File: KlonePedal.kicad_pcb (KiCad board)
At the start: 2 copper layers, 57.5 x 92.1 mm, 68 parts, among them J1 Jack-DC, J2 NMJ4HCD2, J4 NMJ4HCD2, SW1 SW_DPDT_x2, U1 TL072, U2 TL072, U3 MAX1044CPA+

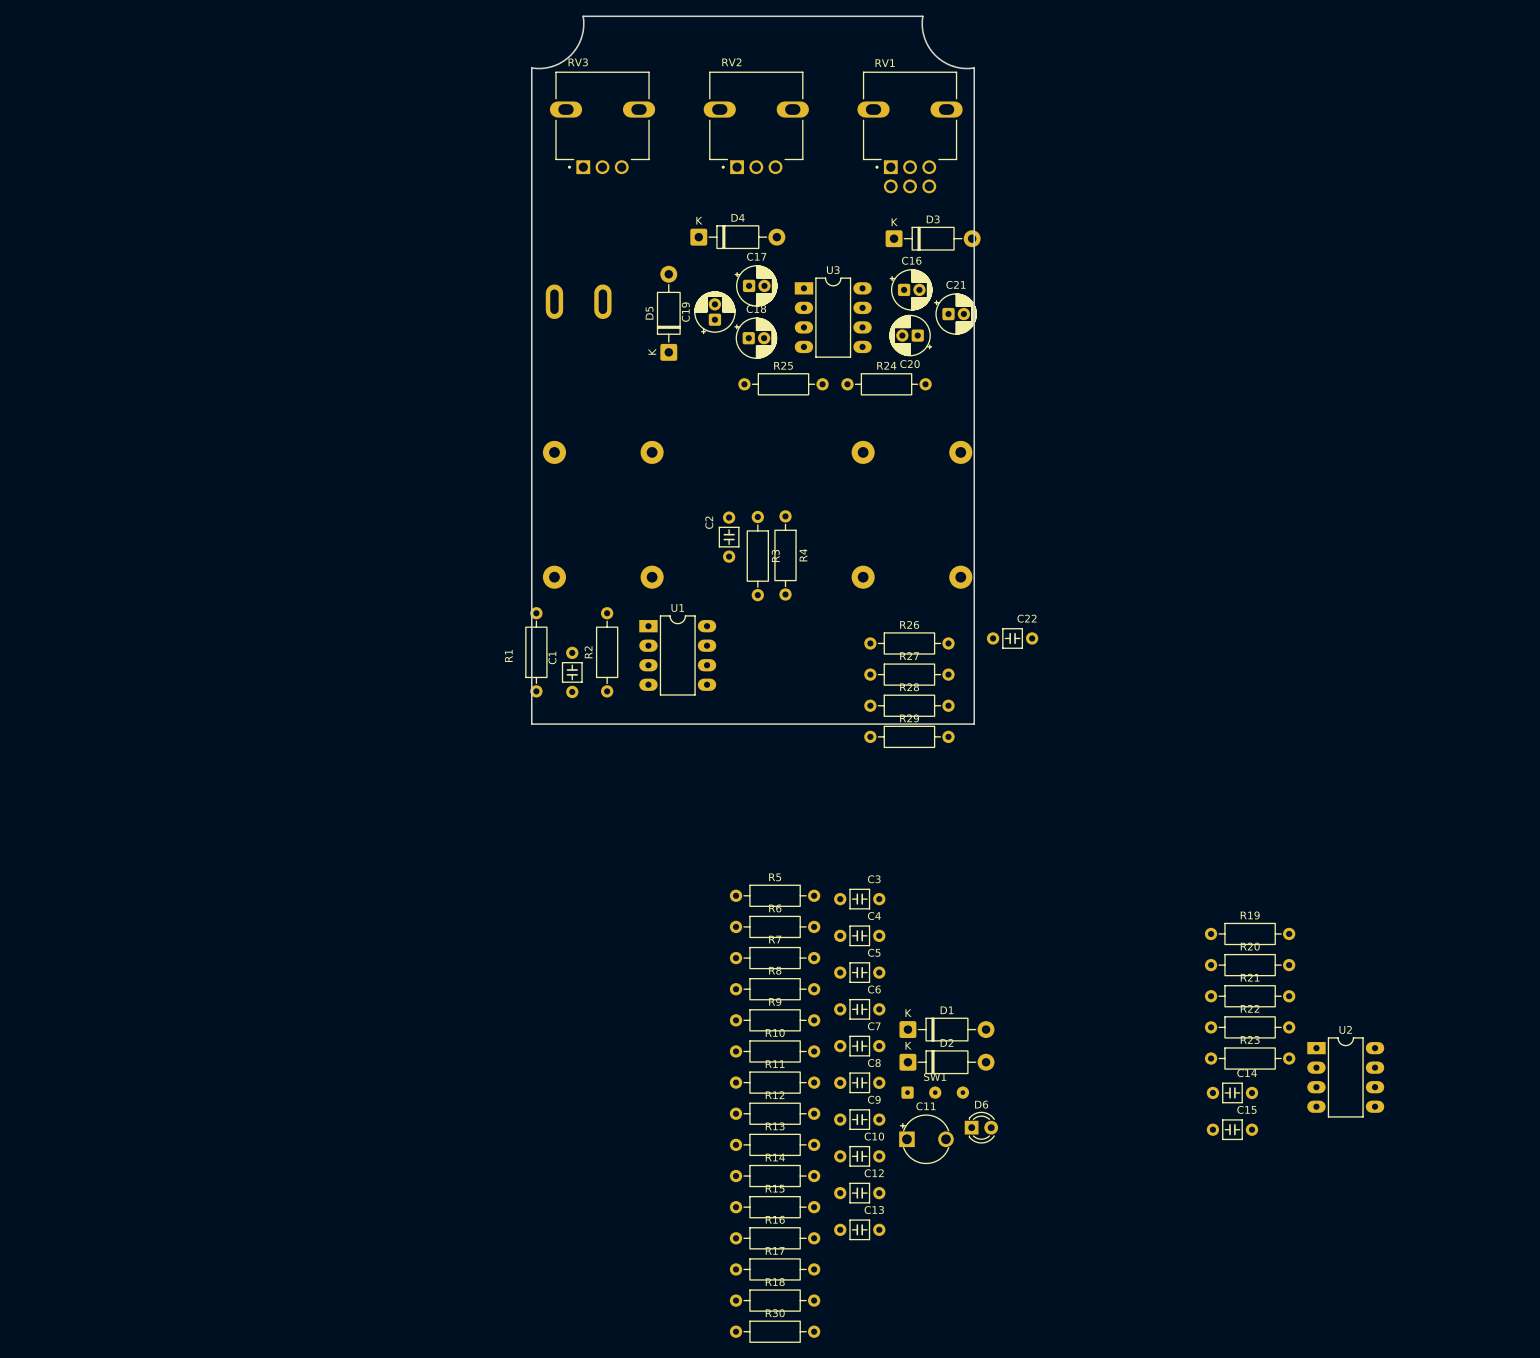
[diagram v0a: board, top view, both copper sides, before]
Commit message: using smt caps and resistors
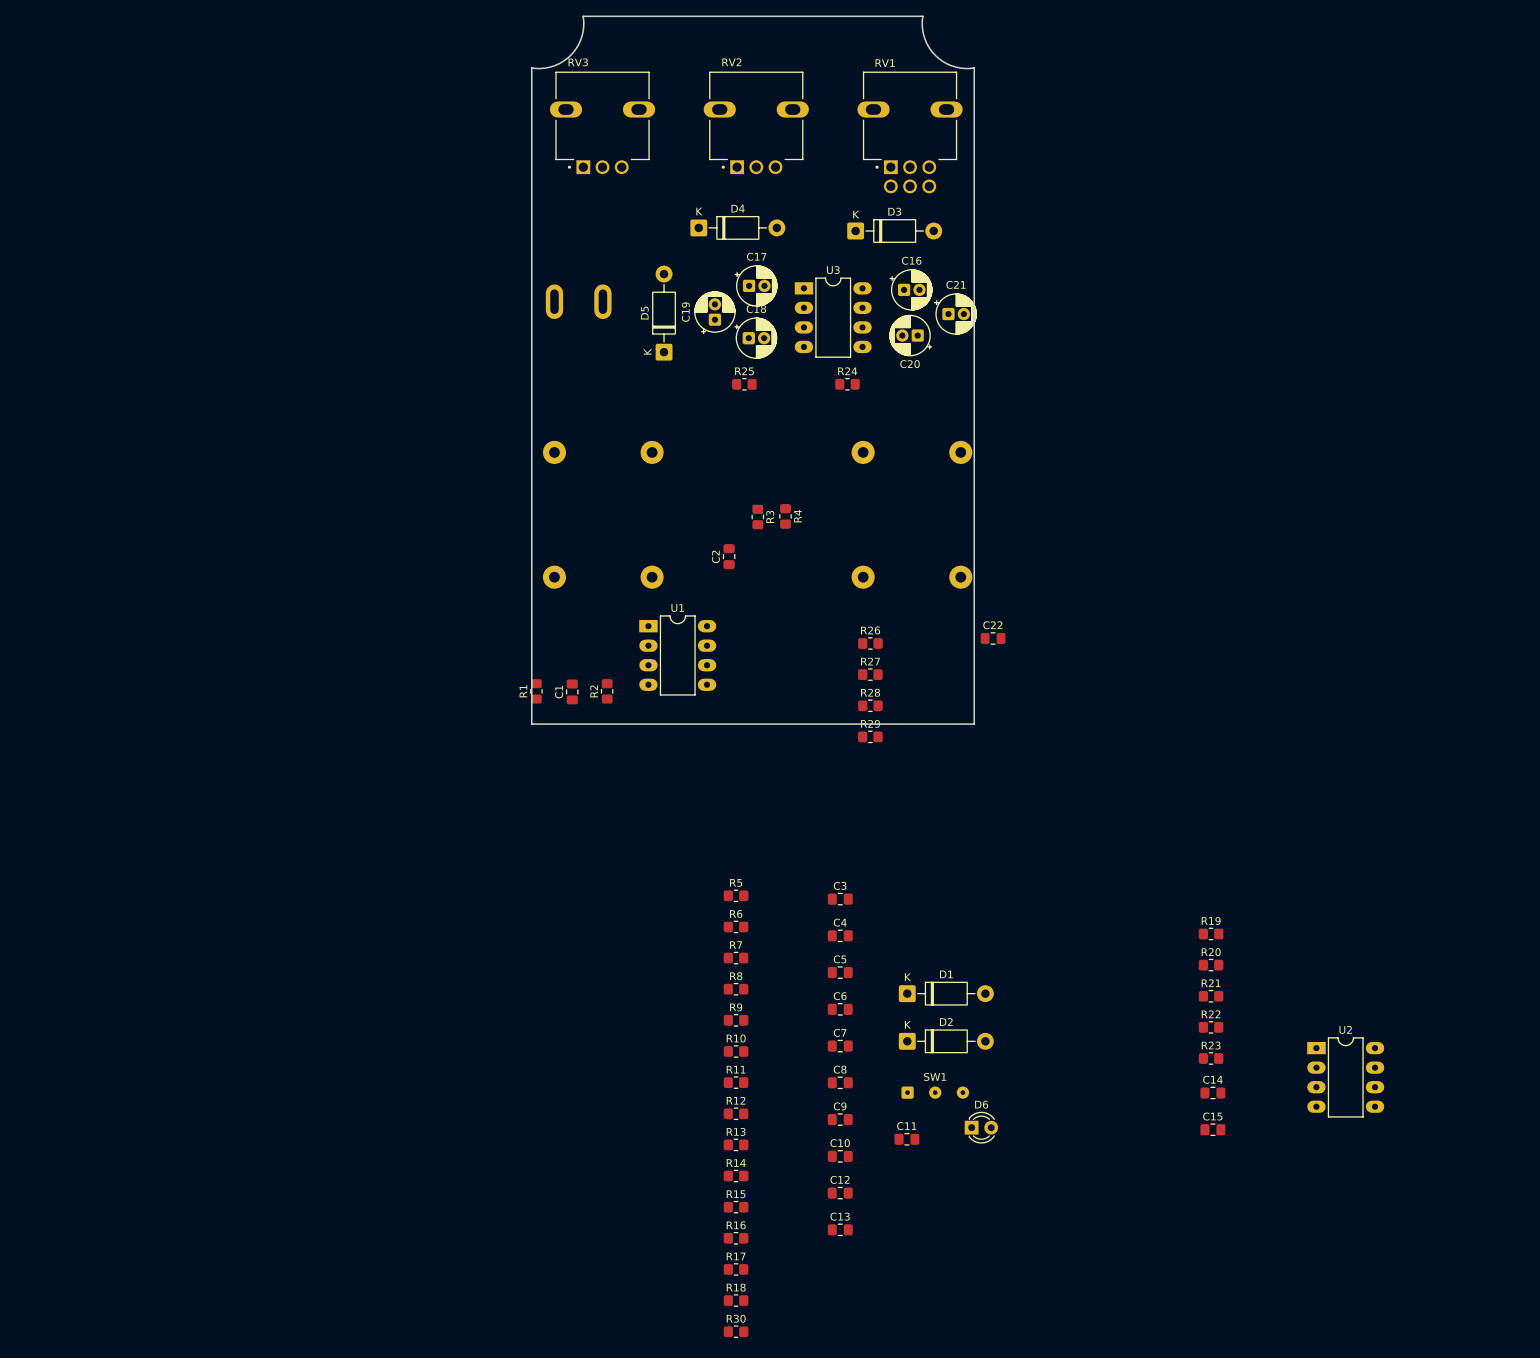
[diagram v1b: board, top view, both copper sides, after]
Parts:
- C1, C10, C12, C13, C14, C15, C2, C22, C3, C4, C5, C6, C7, C8, C9: footprint ECE319K:C_Axial_200mil -> Capacitor_SMD:C_0805_2012Metric_Pad1.18x1.45mm_HandSolder
- C11: footprint ECE319K:CP_Radial_Tantal200mil -> Capacitor_SMD:C_0805_2012Metric_Pad1.18x1.45mm_HandSolder
- R1, R10, R11, R12, R13, R14, R15, R16, R17, R18, R19, R2, R20, R21, R22, R23, R24, R25, R26, R27, R28, R29, R3, R30, R4, R5, R6, R7, R8, R9: footprint Resistor_THT:R_Axial_DIN0207_L6.3mm_D2.5mm_P10.16mm_Horizontal -> Resistor_SMD:R_0805_2012Metric_Pad1.20x1.40mm_HandSolder
- moved D3 5.10 mm to (160.9, 60.8)
- moved D1 4.67 mm to (167.6, 160.0)
- moved D2 2.72 mm to (167.6, 166.2)
- moved D4 1.20 mm to (140.5, 60.4)
- moved D5 0.62 mm to (136.0, 76.6)

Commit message: change metal film resistor footprint
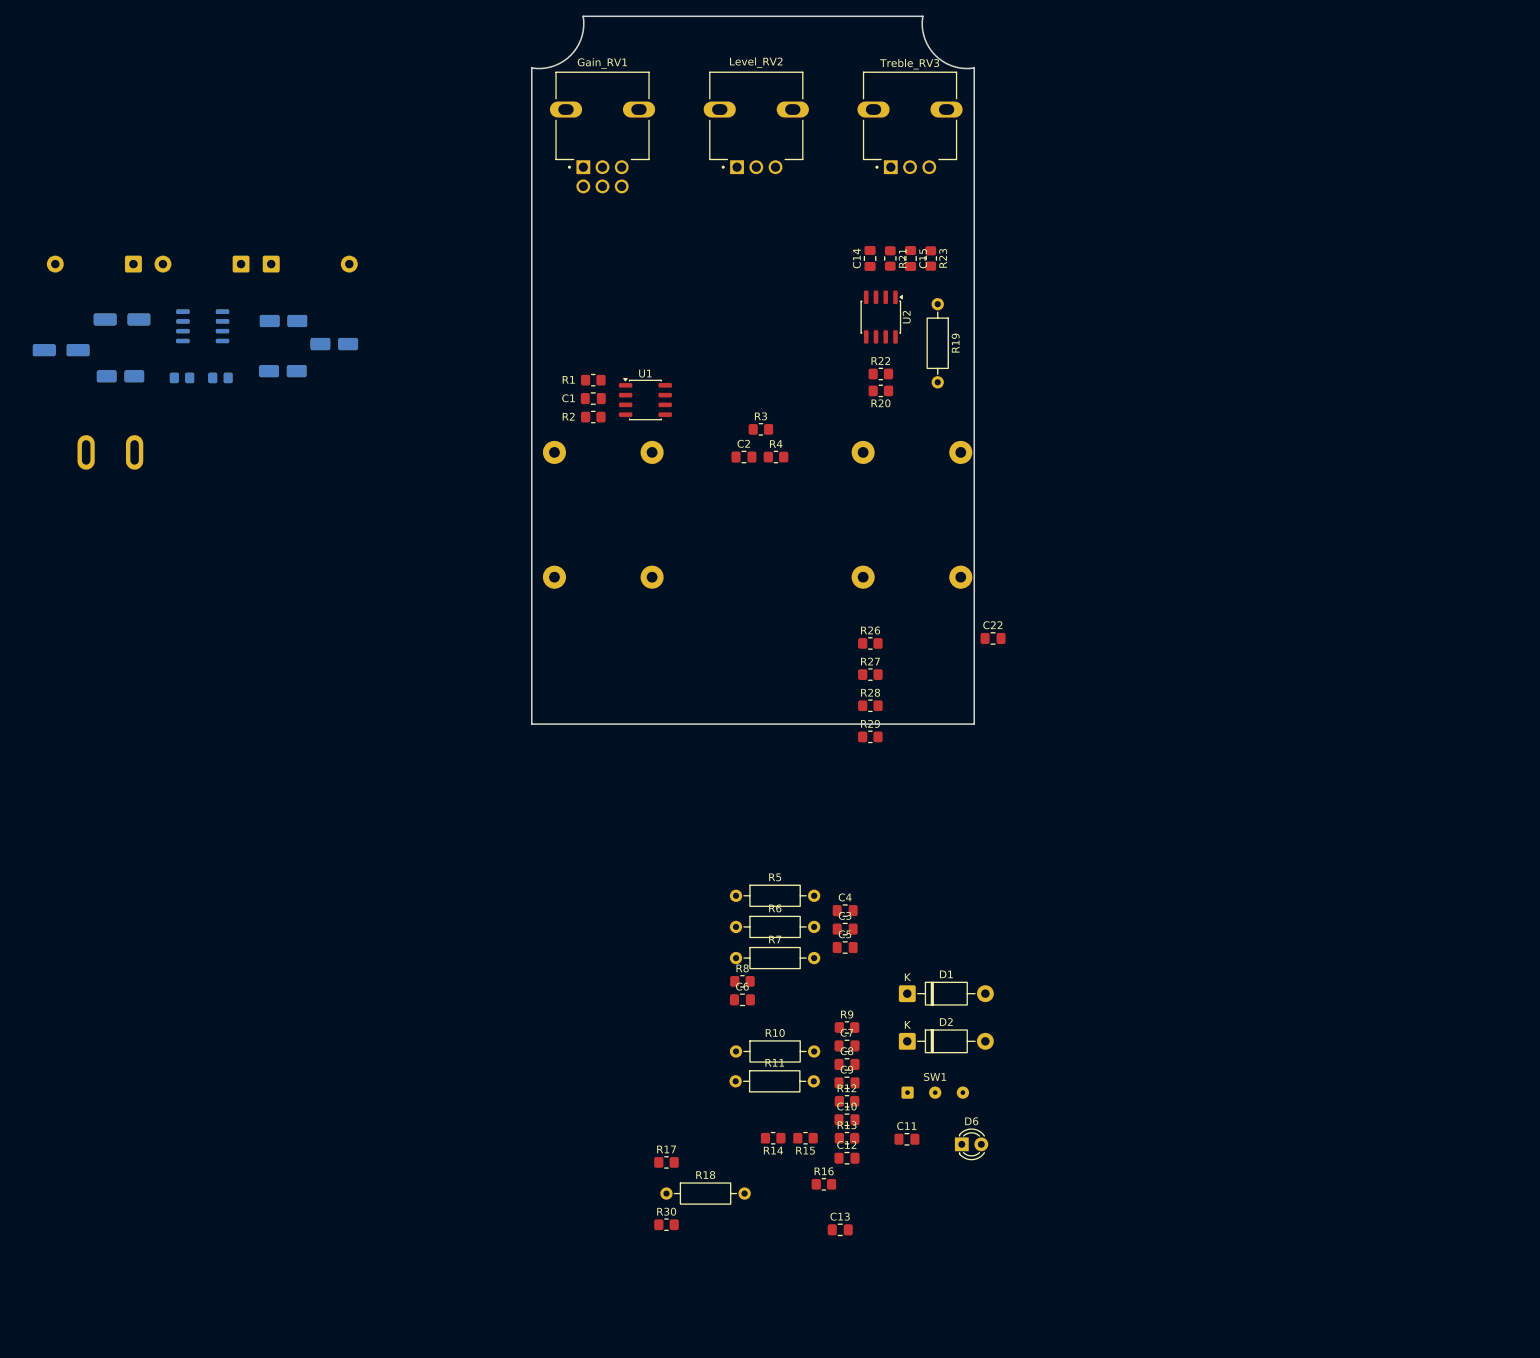
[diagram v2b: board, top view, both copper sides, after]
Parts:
- C16, C21: footprint Capacitor_THT:CP_Radial_D5.0mm_P2.00mm -> Capacitor_SMD:CP_Elec_5x5.4; moved to B.Cu
- C17, C18, C19, C20: footprint Capacitor_THT:CP_Radial_D5.0mm_P2.00mm -> Capacitor_SMD:CP_Elec_4x5.4; moved to B.Cu
- D3, D4, D5, R24, R25: moved to B.Cu
- R10, R11, R18, R19, R5, R6, R7: footprint Resistor_SMD:R_0805_2012Metric_Pad1.20x1.40mm_HandSolder -> Resistor_THT:R_Axial_DIN0207_L6.3mm_D2.5mm_P10.16mm_Horizontal
- U1, U2: footprint ECE319K:DIP-8_W7.62mm_LongPads -> Package_SO:SO-8_3.9x4.9mm_P1.27mm
- U3: footprint ECE319K:DIP-8_W7.62mm_LongPads -> Package_SO:SO-8_3.9x4.9mm_P1.27mm; moved to B.Cu
- moved C15 120.0 mm to (168.1, 64.4), turned to -90 degrees
- moved C14 117.3 mm to (162.8, 64.4), turned to 90 degrees
- moved C21 115.5 mm to (57.6, 76.3), turned to 180 degrees
- moved U2 110.7 mm to (164.2, 72.0), turned to -90 degrees
- moved R23 110.3 mm to (170.7, 64.4), turned to -90 degrees
- moved R21 104.6 mm to (165.4, 64.4), turned to -90 degrees
- moved C20 103.8 mm to (65.3, 79.7), turned to 0 degrees
- moved C16 101.8 mm to (65.5, 72.3), turned to 180 degrees
- moved R22 95.2 mm to (164.2, 79.4)
- moved D3 94.0 mm to (67.0, 65.1), turned to 180 degrees
- moved R19 89.3 mm to (171.6, 70.3), turned to -90 degrees
- moved R24 86.6 mm to (73.3, 79.9), turned to 180 degrees
- moved R20 86.2 mm to (164.2, 81.6), turned to 180 degrees
- moved U3 78.4 mm to (76.0, 73.2), turned to 180 degrees
- moved R25 68.2 mm to (78.3, 79.9), turned to 180 degrees
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- renumbered RV1 to Gain_RV1, RV2 to Level_RV2, RV3 to Treble_RV3

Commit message: add all smd components
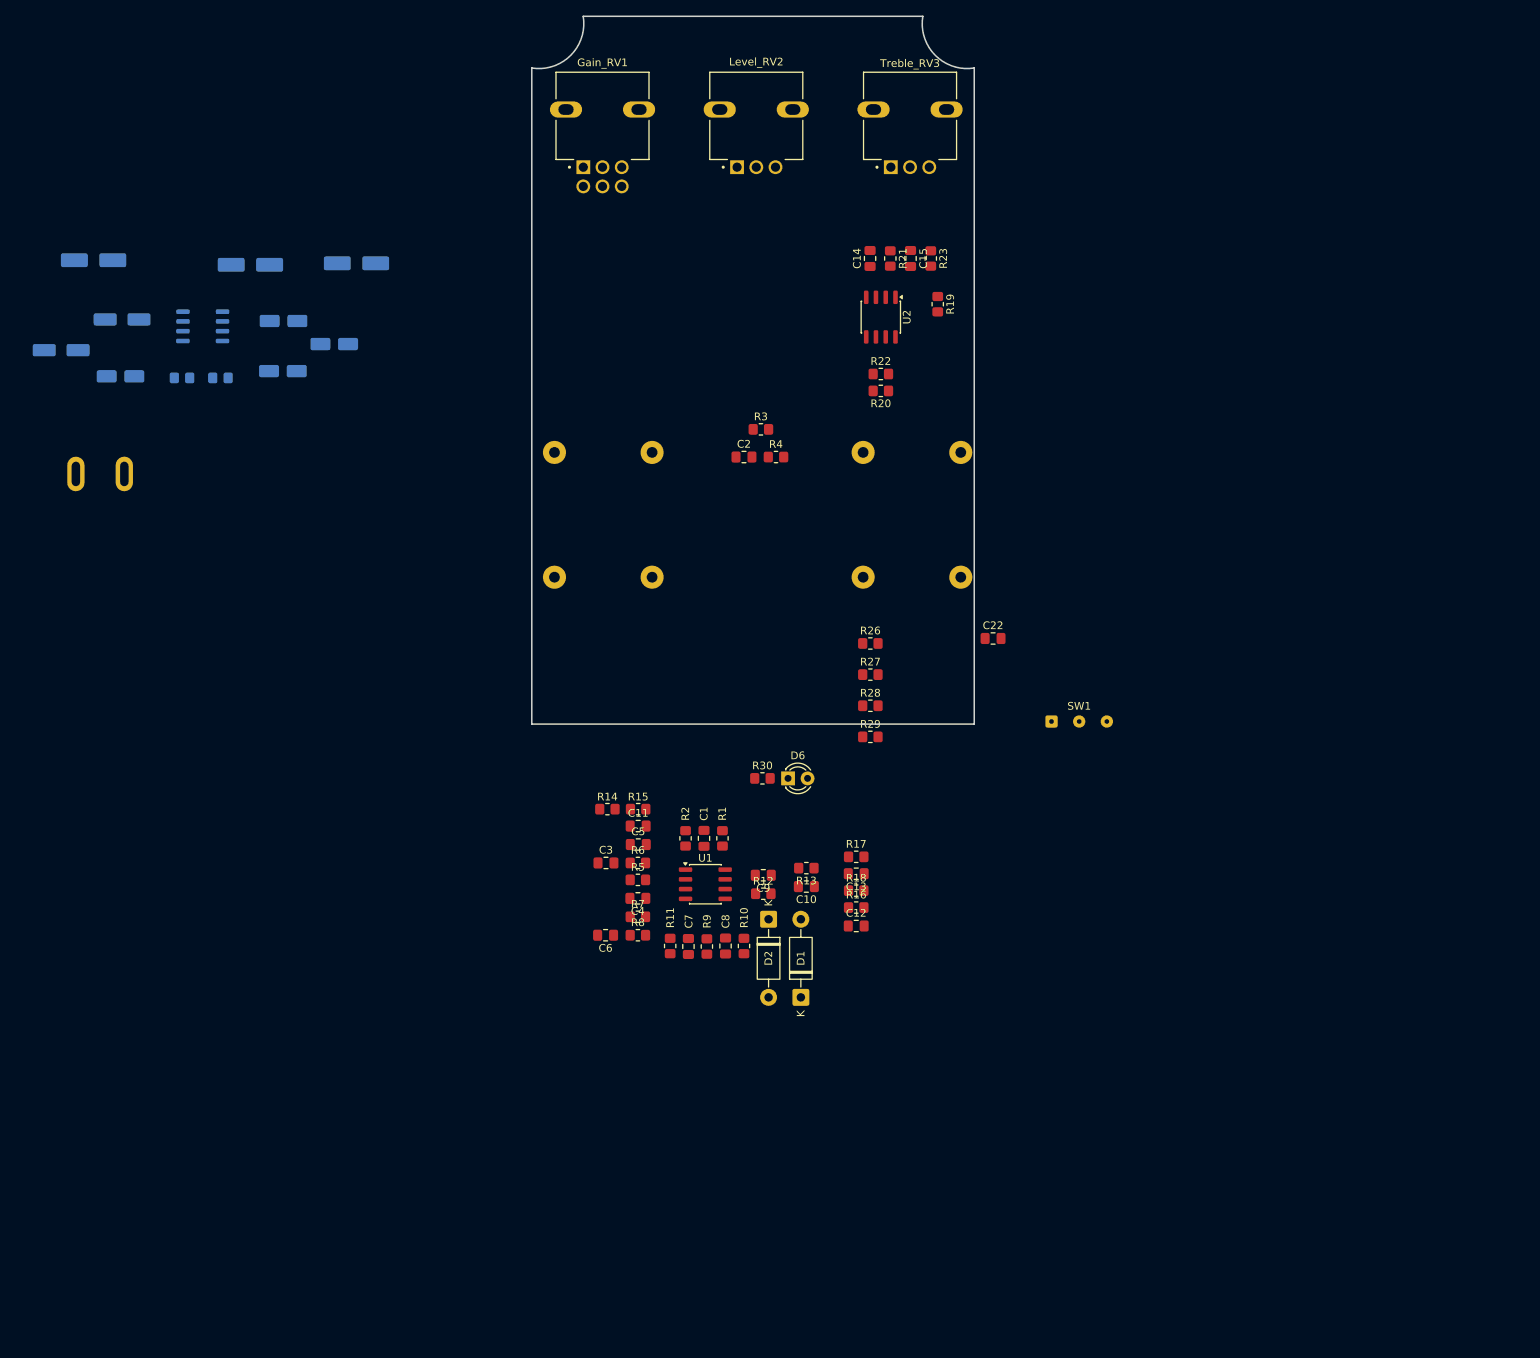
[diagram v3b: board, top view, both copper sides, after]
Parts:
- D3: value 1N4742 -> 1SMA4742; footprint Diode_THT:D_DO-41_SOD81_P10.16mm_Horizontal -> Diode_SMD:D_SMA_Handsoldering
- D4, D5: value 1N4001 -> S1A; footprint Diode_THT:D_DO-41_SOD81_P10.16mm_Horizontal -> Diode_SMD:D_SMA_Handsoldering
- R10, R11, R18, R19, R5, R6, R7: footprint Resistor_THT:R_Axial_DIN0207_L6.3mm_D2.5mm_P10.16mm_Horizontal -> Resistor_SMD:R_0805_2012Metric_Pad1.20x1.40mm_HandSolder
- moved U1 63.5 mm to (141.4, 145.8)
- moved R1 61.9 mm to (143.6, 139.8), turned to -90 degrees
- moved R30 59.4 mm to (148.8, 132.0)
- moved C1 59.0 mm to (141.2, 139.8), turned to -90 degrees
- moved R2 56.1 mm to (138.8, 139.8), turned to -90 degrees
- moved C11 53.7 mm to (132.6, 138.2)
- moved D6 52.7 mm to (152.1, 132.0)
- moved SW1 51.8 mm to (186.4, 124.6)
- moved R15 48.0 mm to (132.6, 136.0)
- moved R14 47.9 mm to (128.6, 136.0)
- moved R17 46.8 mm to (161.0, 142.2)
- moved R18 46.5 mm to (161.0, 146.6)
- moved C13 46.4 mm to (161.0, 144.4), turned to 180 degrees
- moved R16 36.2 mm to (161.0, 148.8)
- moved R13 35.5 mm to (154.5, 143.7), turned to 180 degrees
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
